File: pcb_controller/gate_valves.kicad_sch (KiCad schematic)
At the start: 47 parts, among them J10 22112042, J11 22112042, J12 22112042, J13 22112042, Q5 AO3400A, Q6 AO3400A, Q7 AO3400A, Q8 AO3400A, Q9 AO3400A

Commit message: fix errors in pcb for next version (needs double checking)
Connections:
- net int_vlv1_open renamed rpi_vlv1_open
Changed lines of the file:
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@@
 	(title_block
 		(title "Cryostorage chamber - Gate valve control")
-		(rev "2025-09-12")
+		(rev "2025-09-23")
 		(company "EPFL, Reto Trappitsch")
 	)
@@
 	)
 	(junction
-		(at 40.64 144.78)
-		(diameter 0)
-		(color 0 0 0 0)
-	)
-	(junction
 		(at 71.12 132.08)
 		(diameter 0)
@@
 	(wire
 		(pts
-			(xy 40.64 144.78) (xy 45.72 144.78)
-		)
-		(stroke
-			(width 0)
-			(type default)
-		)
-	)
-	(wire
-		(pts
 			(xy 46.99 99.06) (xy 73.66 99.06)
 		)
@@
 	(wire
 		(pts
+			(xy 38.1 144.78) (xy 45.72 144.78)
+		)
+		(stroke
+			(width 0)
+			(type default)
+		)
+	)
+	(wire
+		(pts
 			(xy 46.99 87.63) (xy 50.8 87.63)
 		)
@@
 	(wire
 		(pts
-			(xy 40.64 140.97) (xy 40.64 144.78)
-		)
-		(stroke
-			(width 0)
-			(type default)
-		)
-	)
-	(wire
-		(pts
 			(xy 86.36 144.78) (xy 95.25 144.78)
 		)
@@
 	(wire
 		(pts
-			(xy 38.1 144.78) (xy 40.64 144.78)
-		)
-		(stroke
-			(width 0)
-			(type default)
-		)
-	)
-	(wire
-		(pts
 			(xy 261.62 99.06) (xy 200.66 99.06)
 		)
@@
 		(pts
 			(xy 201.93 69.85) (xy 204.47 69.85)
-		)
-		(stroke
-			(width 0)
-			(type default)
-		)
-	)
-	(wire
-		(pts
-			(xy 38.1 140.97) (xy 40.64 140.97)
 		)
 		(stroke
@@
 			(effects
 				(font
-					(size 1.27 1.27)
-				)
-				(justify right)
-				(hide yes)
-			)
-		)
-	)
-	(global_label "int_vlv1_open"
-		(shape input)
-		(at 38.1 140.97 180)
-		(fields_autoplaced yes)
-		(effects
-			(font
-				(size 1.27 1.27)
-			)
-			(justify right)
-		)
-		(property "Intersheetrefs" "${INTERSHEET_REFS}"
-			(at 22.3546 140.97 0)
-			(effects
-				(font

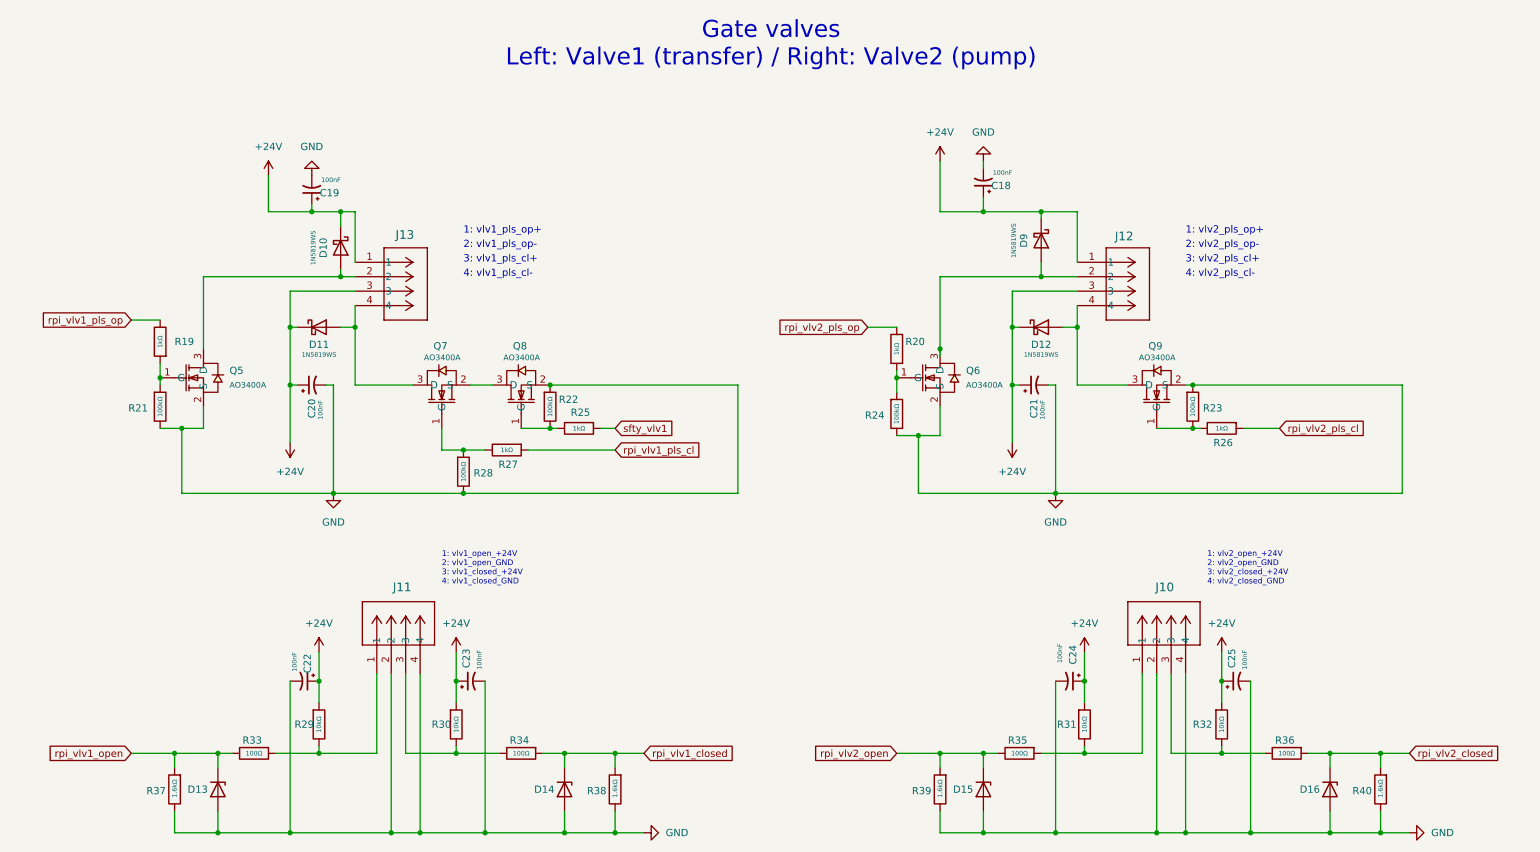
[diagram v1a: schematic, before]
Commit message: revise control board schematic (pcb not yet updated)
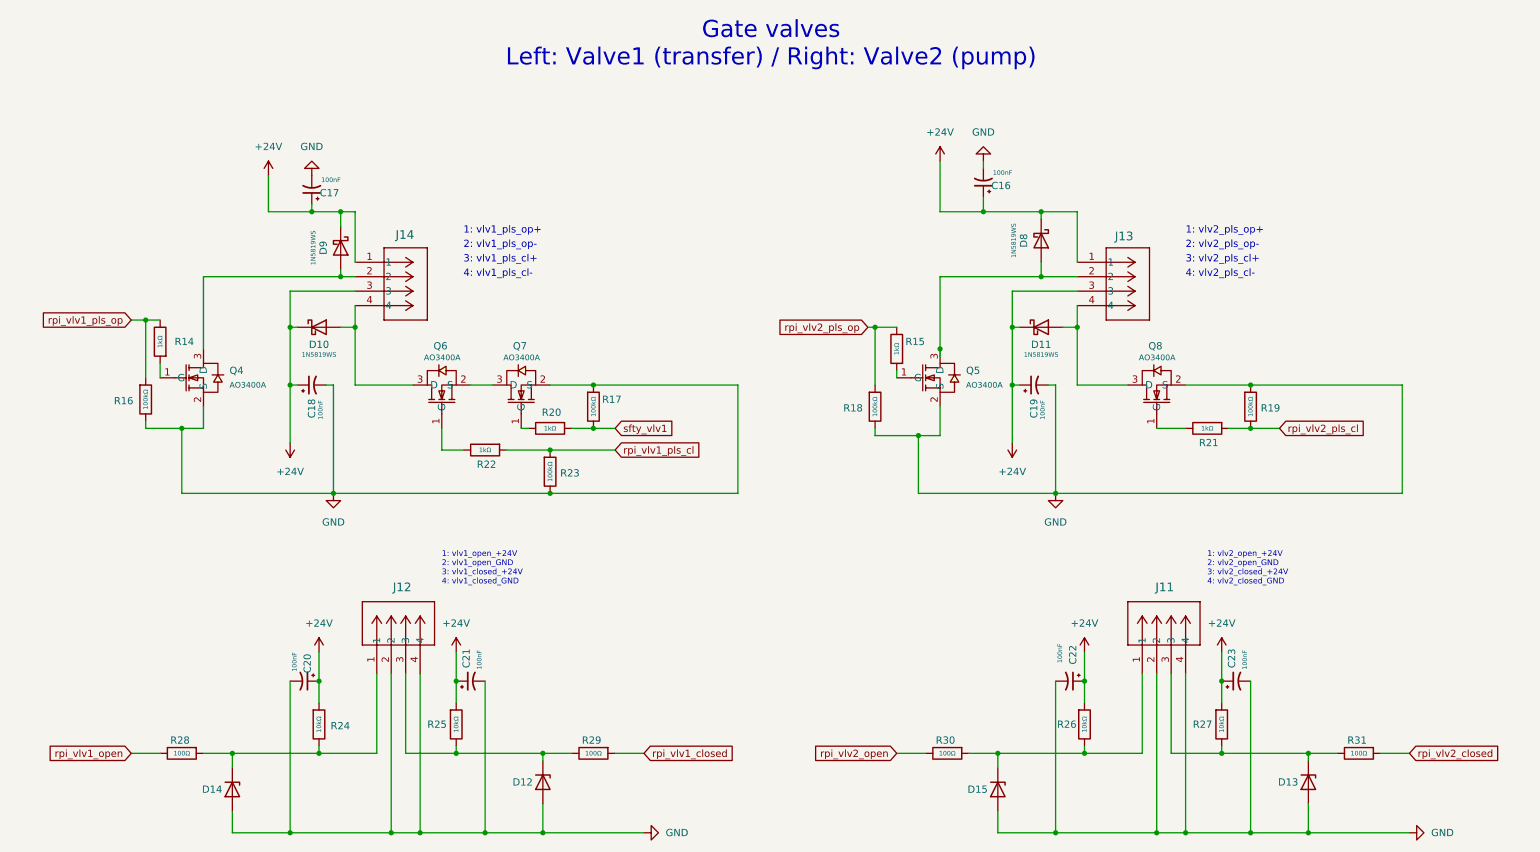
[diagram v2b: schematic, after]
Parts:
- removed R37, R38, R39, R40: 1.6kΩ, PCM_JLCPCB:R_1206, symbol Device:R
- renumbered C18 to C16, C19 to C17, C20 to C18, C21 to C19, C22 to C20, C23 to C21, C24 to C22, C25 to C23, D11 to D10, D12 to D11, D14 to D12, D16 to D13, D13 to D14, D9 to D8, D10 to D9, J10 to J11, J11 to J12, J12 to J13, J13 to J14, Q5 to Q4, Q6 to Q5, Q7 to Q6, Q8 to Q7, Q9 to Q8, R19 to R14, R20 to R15, R21 to R16, R22 to R17, R24 to R18, R23 to R19, R25 to R20, R26 to R21, R27 to R22, R28 to R23, R29 to R24, R30 to R25, R31 to R26, R32 to R27, R33 to R28, R34 to R29, R35 to R30, R36 to R31
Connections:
- net rpi_vlv1_closed: no longer D12.3 (K)
- net rpi_vlv1_open: no longer D14.3 (K)
- net rpi_vlv1_pls_cl: now also R23.1
- net rpi_vlv1_pls_op: now also R16.1
- net rpi_vlv2_closed: no longer D13.3 (K)
- net rpi_vlv2_open: no longer D15.3 (K)
- net rpi_vlv2_pls_cl: now also R19.2
- net rpi_vlv2_pls_op: now also R18.1
- net sfty_vlv1: now also R17.2
- net at Q6.1 (G), R22.2: no longer R23.1
- net at J12.3, R25.2, R29.2: now also D12.3 (K)
- net at Q7.1 (G), R20.2: no longer R17.2
- net at J11.1, R26.2, R30.1: now also D15.3 (K)
- net at Q8.1 (G), R21.2: no longer R19.2
- net at J11.3, R27.2, R31.2: now also D13.3 (K)
- net at J12.1, R24.2, R28.1: now also D14.3 (K)
- net at Q5.1 (G), R15.1: no longer R18.1
- net at Q4.1 (G), R14.1: no longer R16.1
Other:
- moved on the sheet: D12, D13, D14, D15, R16, R17, R18, R19, R20, R21, R22, R23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
